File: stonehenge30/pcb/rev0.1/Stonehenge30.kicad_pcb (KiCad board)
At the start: 2 copper layers, 219.1 x 66.7 mm, 80 parts, among them J1 OLED, J2 Conn_01x03, J3 Conn_01x03, J4 Conn_01x03, SW1 SW_PUSH, SW10 SW_PUSH, SW11 SW_PUSH, SW12 SW_PUSH, SW13 SW_PUSH, SW14 SW_PUSH, SW15 SW_PUSH, SW16 SW_PUSH, SW17 SW_PUSH, SW18 SW_PUSH, SW19 SW_PUSH, SW2 SW_PUSH, SW20 SW_PUSH, SW21 SW_PUSH, SW22 SW_PUSH, SW23 SW_PUSH, SW24 SW_PUSH, SW25 SW_PUSH, SW26 SW_PUSH, SW27 SW_PUSH, SW28 SW_PUSH, SW29 SW_PUSH, SW3 SW_PUSH, SW30 SW_PUSH, SW4 SW_PUSH, SW5 SW_PUSH, SW6 SW_PUSH, SW7 SW_PUSH, SW8 SW_PUSH, SW9 SW_PUSH, U1 ProMicro

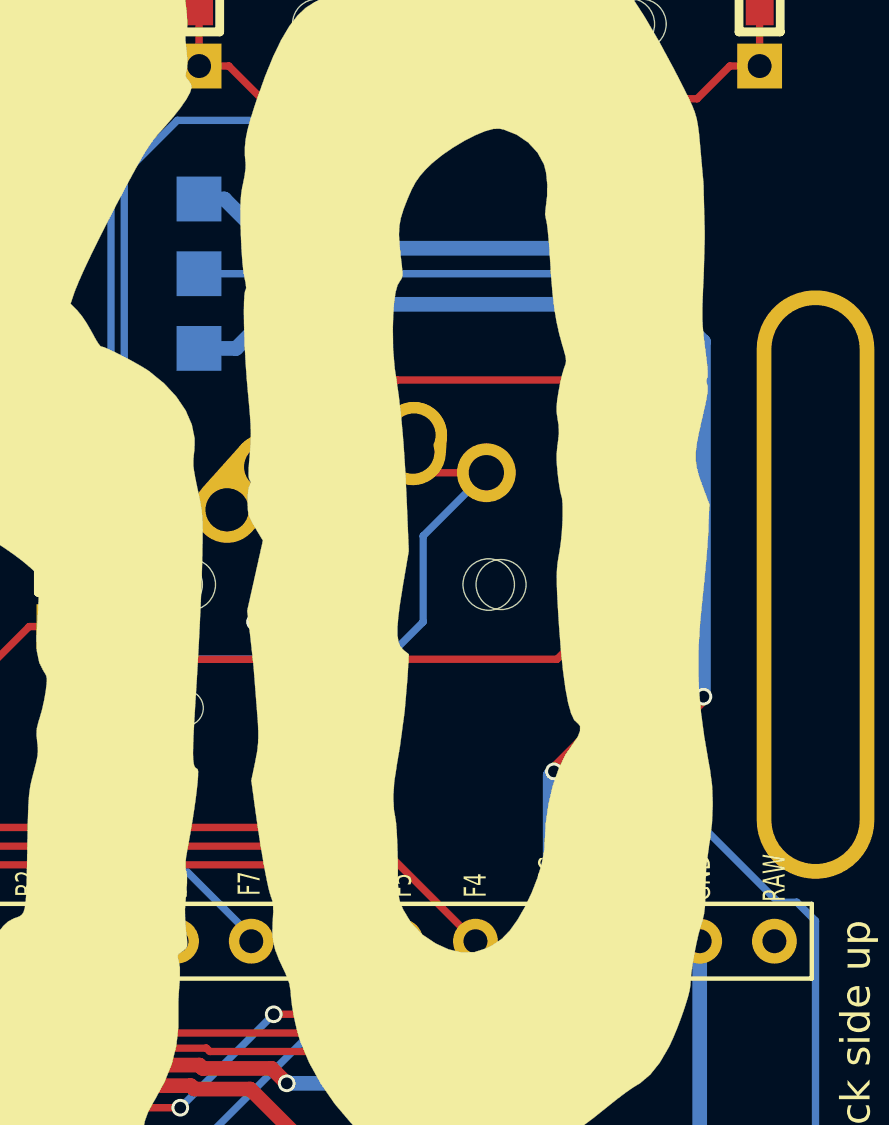
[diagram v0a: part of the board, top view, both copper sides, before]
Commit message: stonehenge30: fixed led line.
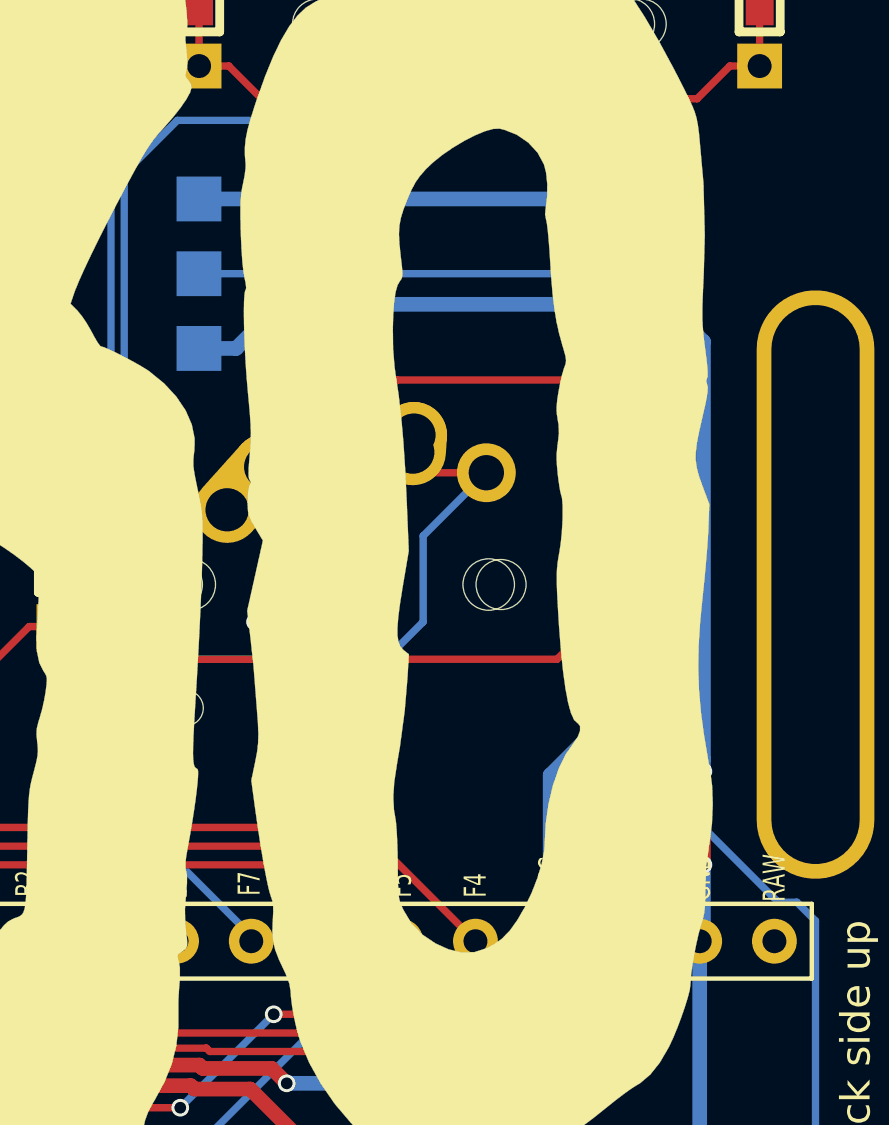
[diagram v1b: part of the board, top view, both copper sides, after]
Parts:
- moved J2 5.08 mm to (252.9, 97.3), turned to 180 degrees
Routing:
- net VCC: track 71.7 -> 66.7 mm, vias 3 -> 1
- net GND: track 91.8 -> 94.3 mm, vias 15 -> 17
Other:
- board text added: "GND DIN 5V"
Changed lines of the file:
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@@
   (general
     (thickness 1.6)
-    (drawings 11)
-    (tracks 717)
+    (drawings 13)
+    (tracks 715)
     (zones 0)
     (modules 80)
@@
   (title_block
     (title Stonehenge30)
-    (date 2018-12-17)
-    (rev 1.1)
+    (date 2019-02-03)
+    (rev 0.2)
     (company marksard)
   )
@@
     (35 F.Paste user)
     (36 B.SilkS user)
-    (37 F.SilkS user)
+    (37 F.SilkS user hide)
     (38 B.Mask user)
     (39 F.Mask user)
@@
   )
   (setup
-    (last_trace_width 0.25)
+    (last_trace_width 0.5)
     (user_trace_width 0.5)
     (trace_clearance 0.2)
@@
   )
   (module kbd:StripLED_back (layer F.Cu)
-    (at 252.9401 92.199)
-    (fp_text reference J2 (at 1.908 0.252 90) (layer Dwgs.User)
+    (at 252.9401 97.279 180)
+    (fp_text reference J2 (at 1.908 0.252 270) (layer Dwgs.User)
       (effects (font (size 1 1) (thickness 0.15)))
     )
-    (fp_text value Conn_01x03 (at 0 7.62) (layer F.Fab) hide
+    (fp_text value Conn_01x03 (at 0 7.62 180) (layer F.Fab) hide
       (effects (font (size 1 1) (thickness 0.15)))
     )
-    (fp_text user LED (at 1.905 0.635 90) (layer B.SilkS)
+    (fp_text user LED (at 1.905 0.635 270) (layer B.SilkS)
       (effects (font (size 1 1) (thickness 0.15)) (justify mirror))
     )
-    (pad 3 smd rect (at 0 0) (size 1.524 1.524) (layers B.Cu B.Paste B.Mask)
+    (pad 3 smd rect (at 0 0 180) (size 1.524 1.524) (layers B.Cu B.Paste B.Mask)
       (net 20 VCC))
-    (pad 2 smd rect (at 0 2.54) (size 1.524 1.524) (layers B.Cu B.Paste B.Mask)
+    (pad 2 smd rect (at 0 2.54 180) (size 1.524 1.524) (layers B.Cu B.Paste B.Mask)
       (net 24 LED))
-    (pad 1 smd rect (at 0 5.08) (size 1.524 1.524) (layers B.Cu B.Paste B.Mask)
+    (pad 1 smd rect (at 0 5.08 180) (size 1.524 1.524) (layers B.Cu B.Paste B.Mask)
       (net 21 GND))
   )
@@
       (xy -4.055928 16.128379) (xy -4.19398 16.082328) (xy -4.372308 16.063401) (xy -4.548563 16.073862)) (layer B.SilkS) (width 0.01))
   )
+  (gr_text "GND\nDIN\n5V" (at 184.3601 113.55876) (layer B.SilkS)
+    (effects (font (size 1.1 1.1) (thickness 0.25)) (justify mirror))
+  )
+  (gr_text "GND\nDIN\n5V" (at 256.1151 94.50876) (layer B.SilkS)
+    (effects (font (size 1.1 1.1) (thickness 0.25)) (justify mirror))
+  )
   (dimension 66.67668 (width 0.3) (layer Dwgs.User)
     (gr_text "66.677 mm" (at 38.90831 105.30304 270) (layer Dwgs.User)
@@
   (segment (start 253.070056 121.748749) (end 255.415089 121.748749) (width 0.5) (layer F.Cu) (net 20))
   (segment (start 240.2401 125.62376) (end 244.230112 121.633748) (width 0.5) (layer F.Cu) (net 20) (status 10))
-  (segment (start 264.87786 111.781) (end 265.0051 111.65376) (width 0.5) (layer B.Cu) (net 20))
-  (segment (start 270.0851 109.11376) (end 268.8151 110.38376) (width 0.5) (layer F.Cu) (net 20))
-  (segment (start 266.2751 110.38376) (end 265.0051 111.65376) (width 0.5) (layer F.Cu) (net 20))
-  (segment (start 268.8151 110.38376) (end 266.2751 110.38376) (width 0.5) (layer F.Cu) (net 20))
-  (segment (start 264.87786 117.4254) (end 264.87786 111.781) (width 0.5) (layer B.Cu) (net 20) (status 10))
-  (via (at 270.0851 109.11376) (size 0.6) (drill 0.4) (layers F.Cu B.Cu) (net 20))
-  (via (at 265.0051 111.65376) (size 0.6) (drill 0.4) (layers F.Cu B.Cu) (net 20))
-  (segment (start 253.80534 92.199) (end 252.9401 92.199) (width 0.5) (layer B.Cu) (net 20) (status 20))
-  (segment (start 255.4801 93.87376) (end 253.80534 92.199) (width 0.5) (layer B.Cu) (net 20))
-  (segment (start 266.9101 93.87376) (end 255.4801 93.87376) (width 0.5) (layer B.Cu) (net 20))
-  (segment (start 270.0851 109.11376) (end 270.0851 97.04876) (width 0.5) (layer B.Cu) (net 20))
-  (segment (start 270.0851 97.04876) (end 266.9101 93.87376) (width 0.5) (layer B.Cu) (net 20))
+  (segment (start 264.87786 111.781) (end 264.87786 117.4254) (width 0.5) (layer B.Cu) (net 20))
+  (segment (start 254.2021 97.279) (end 255.70234 95.77876) (width 0.5) (layer B.Cu) (net 20))
+  (segment (start 252.9401 97.279) (end 254.2021 97.279) (width 0.5) (layer B.Cu) (net 20))
+  (segment (start 255.70234 95.77876) (end 266.096912 95.77876) (width 0.5) (layer B.Cu) (net 20))
+  (segment (start 266.096912 95.77876) (end 268.8151 98.496948) (width 0.5) (layer B.Cu) (net 20))
+  (segment (start 268.8151 98.496948) (end 268.8151 107.84376) (width 0.5) (layer B.Cu) (net 20))
+  (segment (start 268.8151 107.84376) (end 264.87786 111.781) (width 0.5) (layer B.Cu) (net 20))
   (segment (start 269.95786 130.1054) (end 267.41786 132.6454) (width 0.5) (layer B.Cu) (net 21) (status 20))
   (segment (start 269.95786 117.4254) (end 269.95786 130.1054) (width 0.5) (layer B.Cu) (net 21) (status 10))
@@
   (segment (start 254.68122 122.44876) (end 264.87786 132.6454) (width 0.5) (layer F.Cu) (net 21) (status 20))
   (segment (start 246.070101 122.333759) (end 252.665101 122.333759) (width 0.5) (layer F.Cu) (net 21))
-  (segment (start 254.2021 97.279) (end 252.9401 97.279) (width 0.5) (layer B.Cu) (net 21) (status 20))
-  (segment (start 255.70234 95.77876) (end 254.2021 97.279) (width 0.5) (layer B.Cu) (net 21))
-  (segment (start 266.096912 95.77876) (end 255.70234 95.77876) (width 0.5) (layer B.Cu) (net 21))
-  (segment (start 268.8151 98.496948) (end 266.096912 95.77876) (width 0.5) (layer B.Cu) (net 21))
-  (segment (start 269.95786 117.4254) (end 268.8151 116.28264) (width 0.5) (layer B.Cu) (net 21) (status 10))
-  (segment (start 268.8151 116.28264) (end 268.8151 98.496948) (width 0.5) (layer B.Cu) (net 21))
   (via (at 188.64953 129.11614) (size 0.6) (drill 0.4) (layers F.Cu B.Cu) (net 21))
   (via (at 207.70001 129.11614) (size 0.6) (drill 0.4) (layers F.Cu B.Cu) (net 21))
@@
   (via (at 161.5001 111.01876) (size 0.6) (drill 0.4) (layers F.Cu B.Cu) (net 21))
   (via (at 158.9601 98.95376) (size 0.6) (drill 0.4) (layers F.Cu B.Cu) (net 21))
+  (via (at 270.0851 114.82876) (size 0.6) (drill 0.4) (layers F.Cu B.Cu) (net 21))
+  (segment (start 270.0851 117.29816) (end 269.95786 117.4254) (width 0.5) (layer B.Cu) (net 21))
+  (segment (start 270.0851 114.82876) (end 270.0851 117.29816) (width 0.5) (layer B.Cu) (net 21))
+  (via (at 270.0851 111.65376) (size 0.6) (drill 0.4) (layers F.Cu B.Cu) (net 21))
+  (segment (start 270.0851 114.82876) (end 270.0851 111.65376) (width 0.5) (layer F.Cu) (net 21))
+  (segment (start 252.9401 92.199) (end 265.23534 92.199) (width 0.5) (layer B.Cu) (net 21))
+  (segment (start 265.23534 92.199) (end 270.0851 97.04876) (width 0.5) (layer B.Cu) (net 21))
+  (segment (start 270.0851 97.04876) (end 270.0851 111.229496) (width 0.5) (layer B.Cu) (net 21))
+  (segment (start 270.0851 111.229496) (end 270.0851 111.65376) (width 0.5) (layer B.Cu) (net 21))
   (segment (start 259.79786 132.6454) (end 261.1951 131.24816) (width 0.25) (layer B.Cu) (net 22) (status 10))
   (segment (start 261.1951 131.24816) (end 261.1951 122.44876) (width 0.25) (layer B.Cu) (net 22))
